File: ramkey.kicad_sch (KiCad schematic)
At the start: 12 parts, among them SW1 SW_Push, SW2 SW_Push, SW3 SW_Push

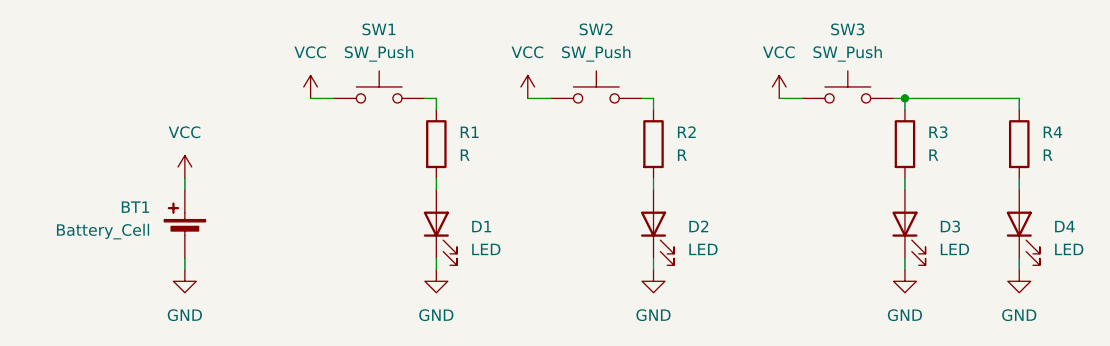
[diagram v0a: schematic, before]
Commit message: feat: add silkscreen
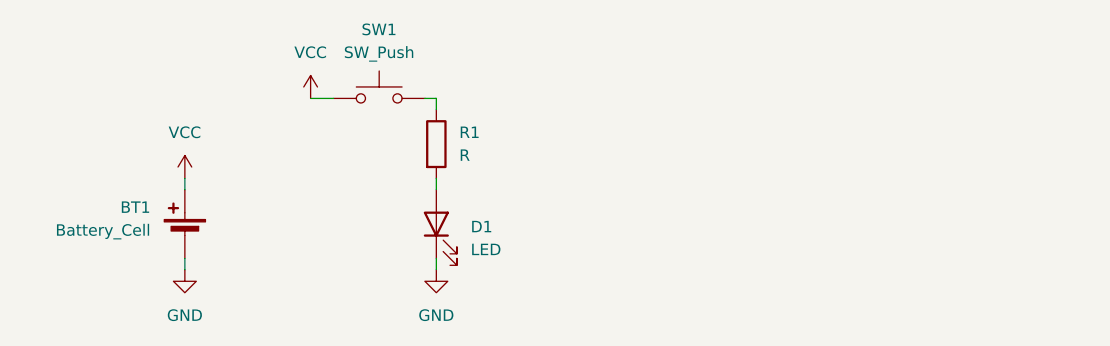
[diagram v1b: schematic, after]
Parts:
- removed D2, D3, D4: LED, LED_THT:LED_D3.0mm, symbol Device:LED
- removed R2, R3, R4: R, Resistor_THT:R_Axial_DIN0207_L6.3mm_D2.5mm_P7.62mm_Horizontal, symbol Device:R
- removed SW2, SW3: SW_Push, Button_Switch_THT:SW_PUSH_6mm, symbol Switch:SW_Push
